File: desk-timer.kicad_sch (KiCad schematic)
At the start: 0 parts

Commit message: Add wired desk timer schematic and project documentation
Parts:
- added BZ1: PS1240P02BT, Buzzer_Beeper:Buzzer_TDK_PS1240P02BT_D12.2mm_H6.5mm, symbol Device:Buzzer
- added C1: 1uF >=16V, Capacitor_SMD:C_1206_3216Metric_Pad1.33x1.80mm_HandSolder, symbol Device:C
- added C2: 100nF, Capacitor_THT:C_Disc_D5.0mm_W2.5mm_P2.50mm, symbol Device:C
- added D1, D2, D3, D4, D5, D6: WP7113GD, LED_THT:LED_D5.0mm, symbol Device:LED
- added R1, R2, R3, R4, R5, R6: 680, Resistor_SMD:R_1206_3216Metric_Pad1.30x1.75mm_HandSolder, symbol Device:R
- added R7: 330, Resistor_SMD:R_1206_3216Metric_Pad1.30x1.75mm_HandSolder, symbol Device:R
- added R8: 100k, Resistor_SMD:R_1206_3216Metric_Pad1.30x1.75mm_HandSolder, symbol Device:R
- added SW1, SW2: B3F-1000, Button_Switch_THT:SW_TH_Tactile_Omron_B3F-100x, symbol Switch:SW_Push
- added U1: Arduino_Nano_v3.x, Module:Arduino_Nano, symbol MCU_Module:Arduino_Nano_v3.x
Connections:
- new net: BZ1.1 (+), C1.2, R8.1
- new net: D5.2 (A), R5.2
- new net: D1.2 (A), R1.2
- new net: D6.2 (A), R6.2
- new net: C1.1, R7.2
- new net: D2.2 (A), R2.2
- new net: D3.2 (A), R3.2
- new net: D4.2 (A), R4.2
- new net +5V: C2.1, U1.27 (+5V)
- new net BTN_RESET: SW2.1, U1.12 (D9)
- new net BTN_START: SW1.1, U1.11 (D8)
- new net BUZZER: R7.1, U1.13 (D10)
- new net GND: BZ1.2 (-), C2.2, D1.1 (K), D2.1 (K), D3.1 (K), D4.1 (K), D5.1 (K), D6.1 (K), R8.2, SW1.2, SW2.2, U1.29 (GND), U1.4 (GND)
- new net LED1: R1.1, U1.5 (D2)
- new net LED2: R2.1, U1.6 (D3)
- new net LED3: R3.1, U1.7 (D4)
- new net LED4: R4.1, U1.8 (D5)
- new net LED5: R5.1, U1.9 (D6)
- new net LED6: R6.1, U1.10 (D7)
- no-connect marks 0 -> 18
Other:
- note added: "01 USB-powered Arduino Nano"
- note added: "02 Six progress LEDs / active HIGH"
- note added: "03 Buttons / active LOW"
- note added: "04 AC-coupled passive piezo"
- note added: "C1: non-polar ceramic (X7R suggested). R8 discharges the piezo; no DC bias in steady state. Firmware: tone(D10, 4000); verify loudness on prototype."
- note added: "DESK TIMER / 25 MINUTES"
- note added: "Each LED has its own 680 ohm resistor. All resistors: 1206 hand-solder footprint, 0.25 W."
- note added: "Firmware: INPUT_PULLUP on D8/D9; debounce buttons. SW2 resets the timer in software, not the Nano RESET pin."
- note added: "RESET TIMER"
- note added: "START / PAUSE"
- note added: "USB powers the Nano and +5V rail. Fit two 1x15 female headers at U1. Verify Nano model and 15.24 mm row spacing."
- title: (none) -> Desk Timer - 25 minute focus timer

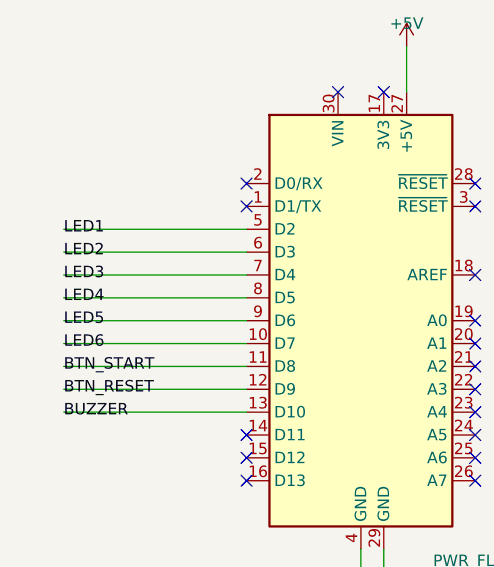
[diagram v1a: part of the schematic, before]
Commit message: Complete desk timer PCB layout and routing
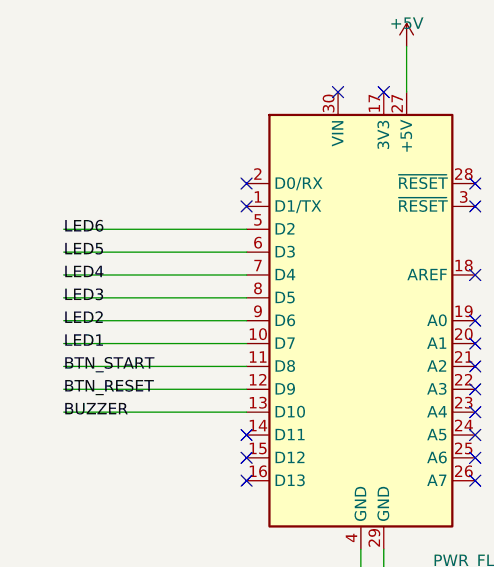
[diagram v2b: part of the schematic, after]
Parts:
- C2: footprint Capacitor_THT:C_Disc_D5.0mm_W2.5mm_P2.50mm -> Capacitor_SMD:C_1206_3216Metric_Pad1.33x1.80mm_HandSolder
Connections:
- net LED1: now also U1.10 (D7); no longer U1.5 (D2)
- net LED2: now also U1.9 (D6); no longer U1.6 (D3)
- net LED3: now also U1.8 (D5); no longer U1.7 (D4)
- net LED4: now also U1.7 (D4); no longer U1.8 (D5)
- net LED5: now also U1.6 (D3); no longer U1.9 (D6)
- net LED6: now also U1.5 (D2); no longer U1.10 (D7)
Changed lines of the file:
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@@
     )
   )
-  (label "LED1"
+  (label "LED6"
     (at 30.48 66.04 0)
     (effects
@@
     )
   )
-  (label "LED2"
+  (label "LED5"
     (at 30.48 68.58 0)
     (effects
@@
     )
   )
-  (label "LED3"
+  (label "LED4"
     (at 30.48 71.12 0)
     (effects
@@
     )
   )
-  (label "LED4"
+  (label "LED3"
     (at 30.48 73.66 0)
     (effects
@@
     )
   )
-  (label "LED5"
+  (label "LED2"
     (at 30.48 76.2 0)
     (effects
@@
     )
   )
-  (label "LED6"
+  (label "LED1"
     (at 30.48 78.74 0)
     (effects
@@
       )
     )
-    (property "Footprint" "Capacitor_THT:C_Disc_D5.0mm_W2.5mm_P2.50mm"
+    (property "Footprint" "Capacitor_SMD:C_1206_3216Metric_Pad1.33x1.80mm_HandSolder"
       (at 91.44 63.5 0)
       (effects
